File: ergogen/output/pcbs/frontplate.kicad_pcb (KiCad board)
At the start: 2 copper layers, 133.3 x 91.7 mm, 5 parts

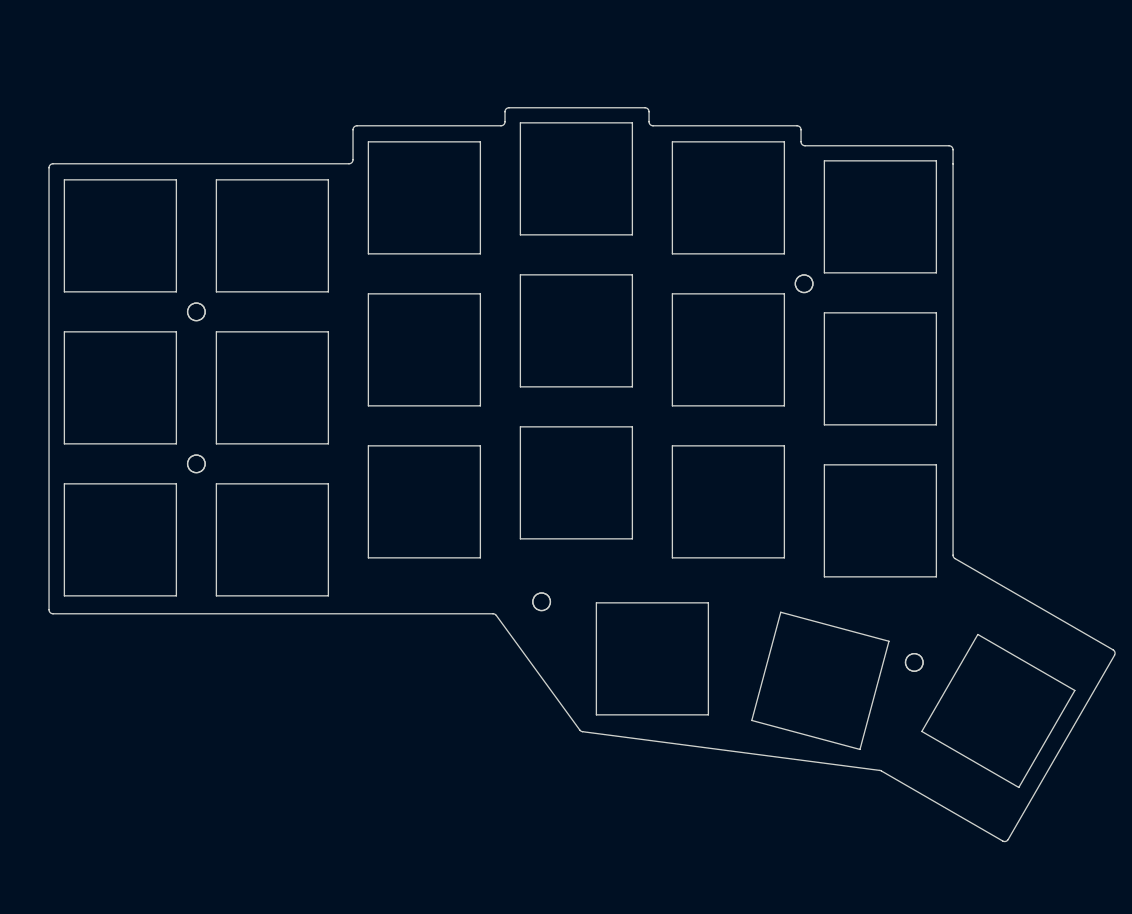
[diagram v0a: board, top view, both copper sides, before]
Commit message: Removed outer column
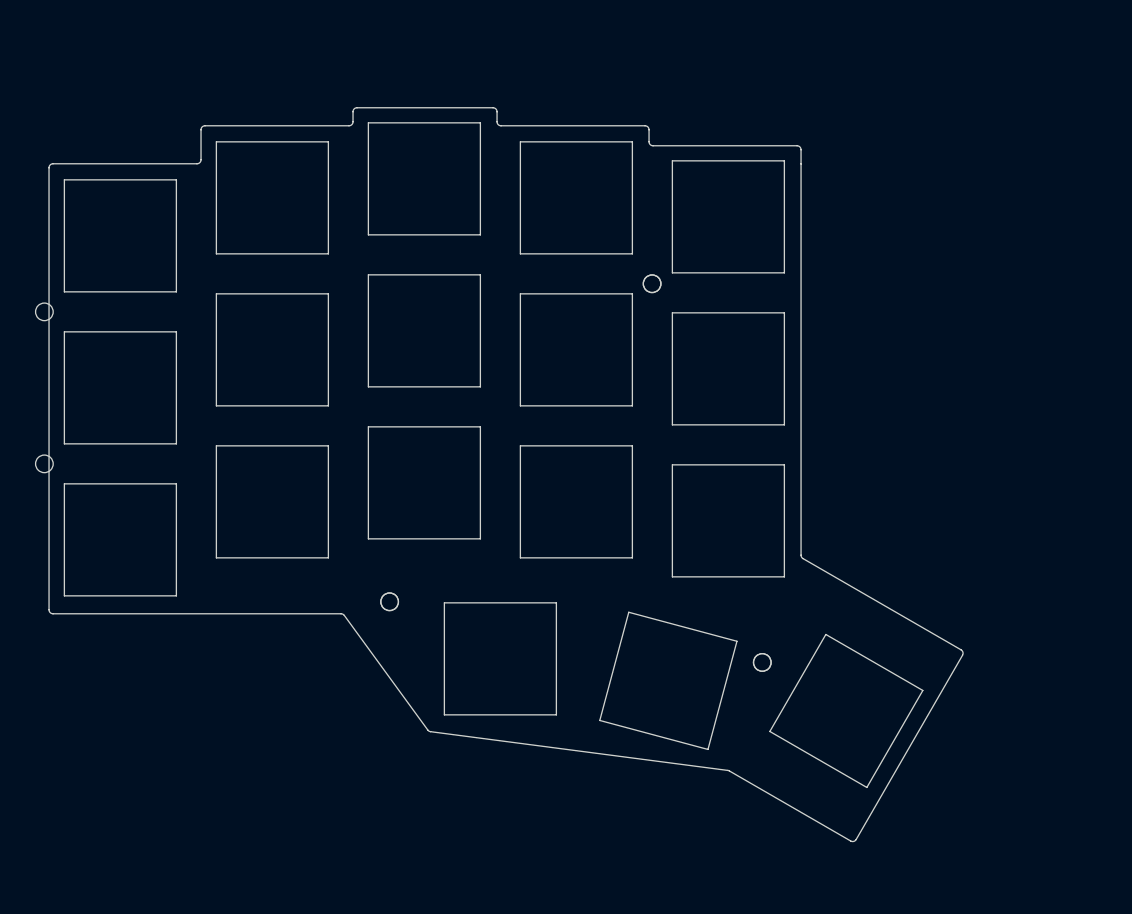
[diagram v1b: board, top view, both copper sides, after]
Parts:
- moved MH5 19.0 mm to (180.2, 115.3)
- moved MH1 19.0 mm to (90.5, 71.5)
- moved MH2 19.0 mm to (90.5, 90.5)
- moved MH3 19.0 mm to (166.5, 68.0)
- moved MH4 19.0 mm to (133.7, 107.7)
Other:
- board size 133.3 x 91.7 mm -> 114.3 x 91.7 mm

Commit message: Changed stagger to be like karia
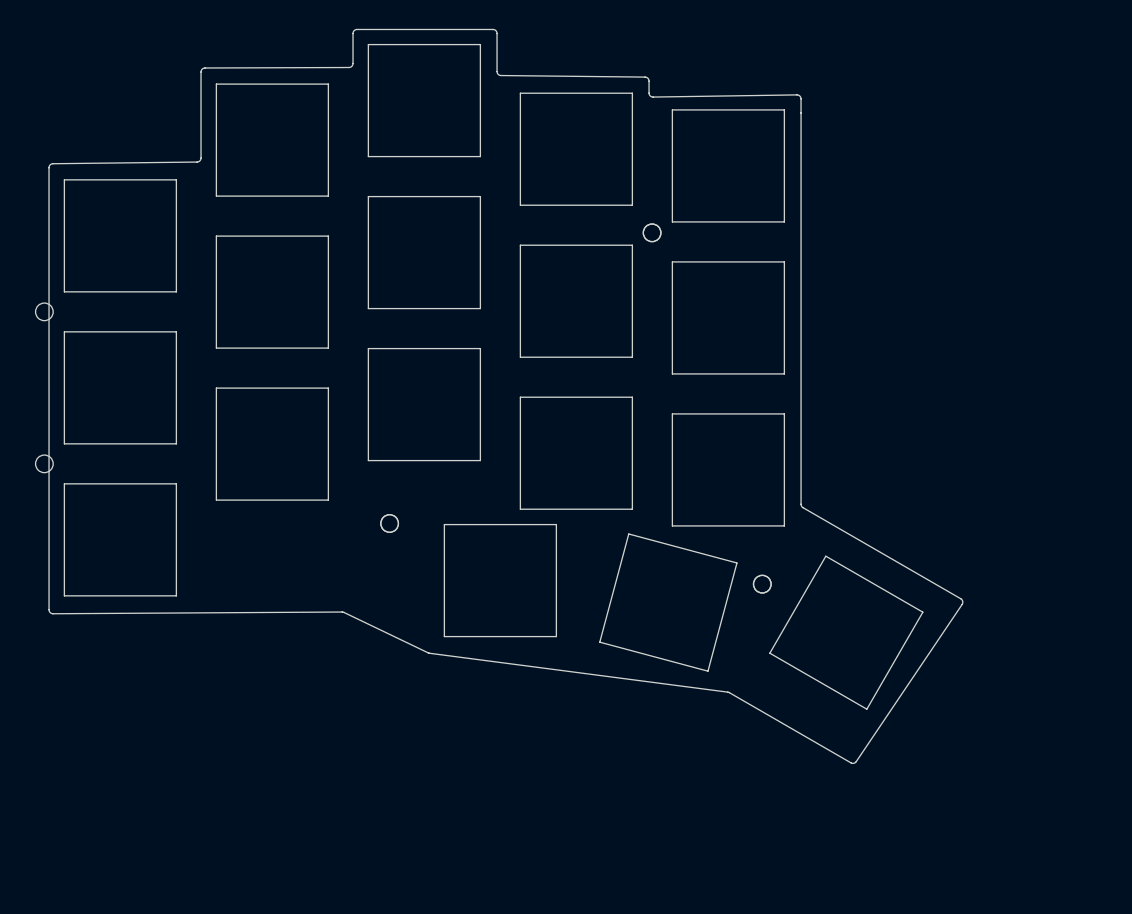
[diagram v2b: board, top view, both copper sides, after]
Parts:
- moved MH4 9.78 mm to (133.7, 98.0)
- moved MH5 9.78 mm to (180.2, 105.5)
- moved MH3 6.36 mm to (166.5, 61.6)
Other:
- board size 114.3 x 91.7 mm -> 114.2 x 91.7 mm

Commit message: Added splay to pinky
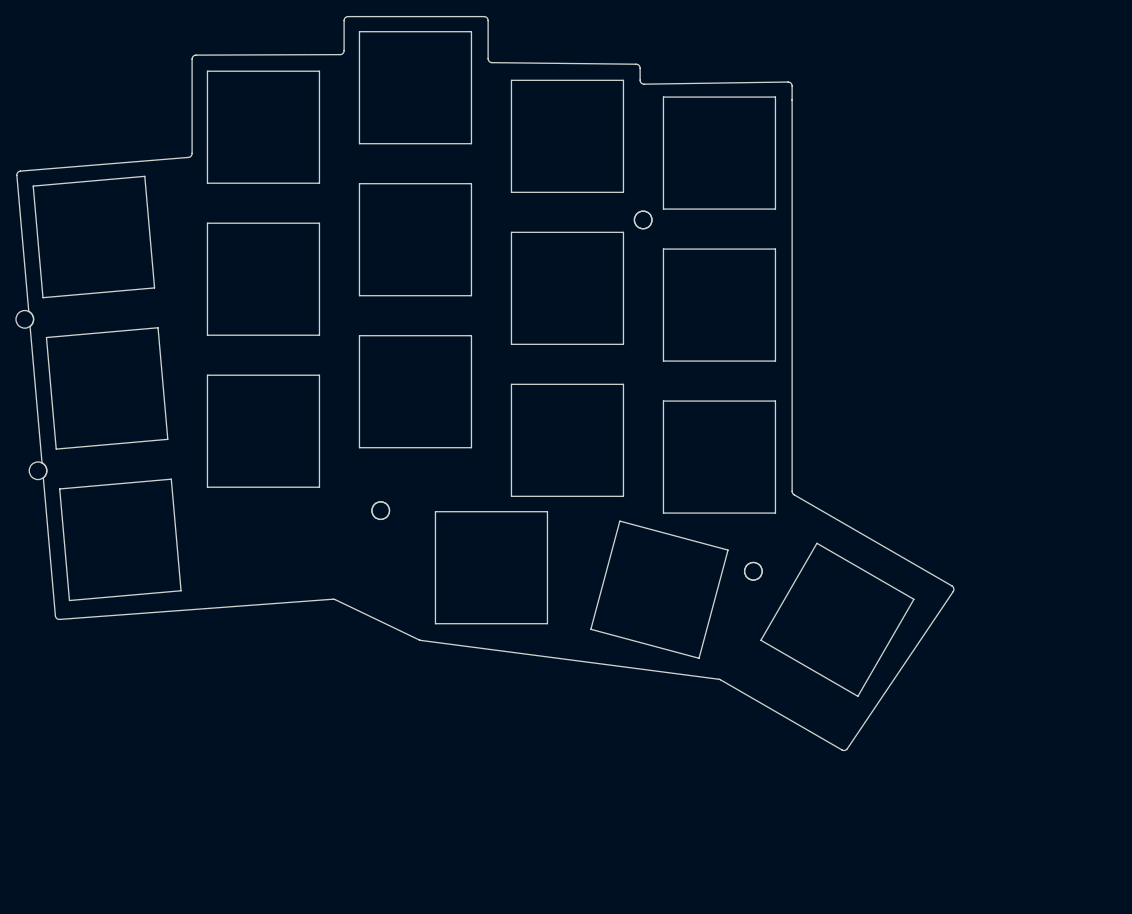
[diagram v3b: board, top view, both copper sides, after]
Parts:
- moved MH1 2.62 mm to (88.1, 72.4), turned to 5 degrees
- moved MH4 1.96 mm to (132.5, 96.3)
- moved MH5 1.96 mm to (179.1, 103.9)
- moved MH3 1.96 mm to (165.4, 60.0)
- moved MH2 1.17 mm to (89.7, 91.4), turned to 5 degrees
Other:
- board size 114.2 x 91.7 mm -> 117.1 x 91.7 mm

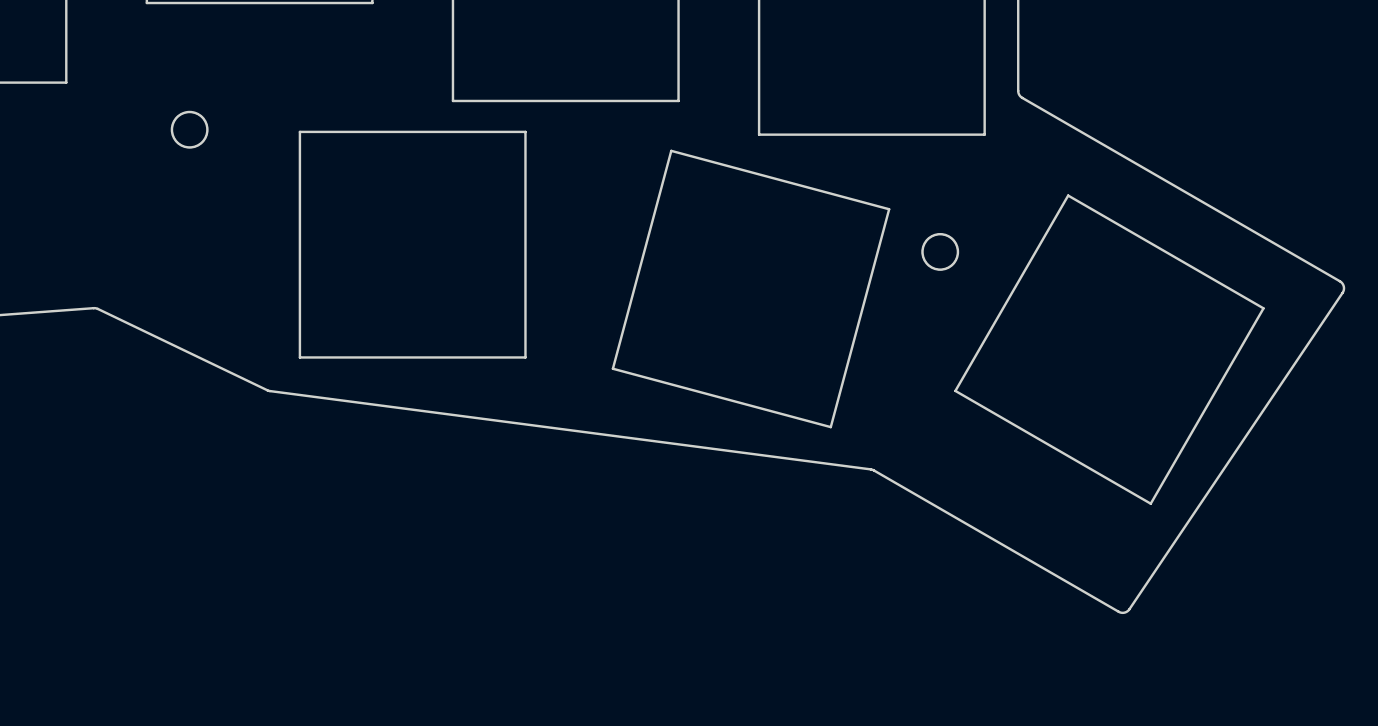
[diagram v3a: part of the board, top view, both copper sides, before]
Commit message: Changed thumb key back to 1u
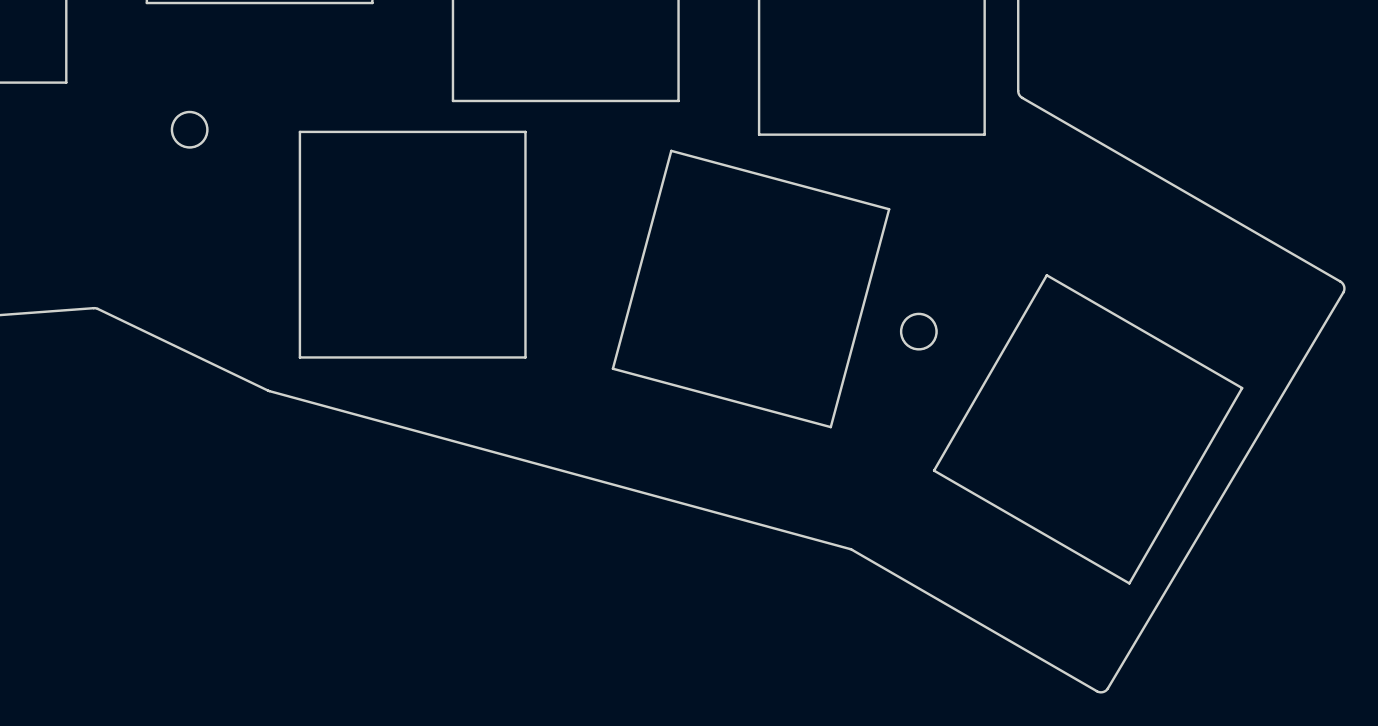
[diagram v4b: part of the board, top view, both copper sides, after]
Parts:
- moved MH5 5.12 mm to (177.8, 108.9)
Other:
- board size 117.1 x 91.7 mm -> 117.2 x 96.7 mm
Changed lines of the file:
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@@
   )
   (module "ceoloide:mounting_hole_npth" (layer F.Cu)
-      (at 179.1254966 103.9282479 60)
+      (at 177.7998255 108.87572 60)
       (fp_text reference "MH5" (at 0 2.55 60) (layer F.SilkS) hide (effects (font (size 1 1) (thickness 0.15))))
       (pad "" np_thru_hole circle (at 0 0 60) (size 2.2 2.2) (drill 2.2) (layers *.Cu *.Mask))
@@
 (gr_line (start 183.96667038015485 43.26992130873259) (end 183.96744510000002 45.01459040003829) (layer Edge.Cuts) (stroke (width 0.15) (type default)))
 (gr_line (start 183.9674451 45.01481240004068) (end 183.9674451 93.93435851661681) (layer Edge.Cuts) (stroke (width 0.15) (type default)))
-(gr_line (start 184.2174451 94.36737121661682) (end 203.93834540973833 105.75323831890144) (layer Edge.Cuts) (stroke (width 0.15) (type default)))
-(gr_line (start 204.1030141097383 106.46562511890141) (end 190.86864454351888 126.1091037392597) (layer Edge.Cuts) (stroke (width 0.15) (type default)))
-(gr_line (start 190.2039758435189 126.26274233925969) (end 175.00808706223265 117.48939183913699) (layer Edge.Cuts) (stroke (width 0.15) (type default)))
-(gr_line (start 174.82271206223268 117.42659853913699) (end 137.52391425873893 112.56494858875345) (layer Edge.Cuts) (stroke (width 0.15) (type default)))
-(gr_line (start 137.3721942392345 112.5199139793924) (end 126.84466306000907 107.46728833906016) (layer Edge.Cuts) (stroke (width 0.15) (type default)))
+(gr_line (start 184.2174451 94.36737121661682) (end 203.9637846754554 105.76792568581091) (layer Edge.Cuts) (stroke (width 0.15) (type default)))
+(gr_line (start 204.14352157545537 106.45652828581092) (end 189.53461200661957 131.0192645320555) (layer Edge.Cuts) (stroke (width 0.15) (type default)))
+(gr_line (start 188.85487510661957 131.19668733205543) (end 173.65217521437293 122.41940443517655) (layer Edge.Cuts) (stroke (width 0.15) (type default)))
+(gr_line (start 173.53339681437296 122.36994343517657) (end 137.4884527110838 112.56655937095502) (layer Edge.Cuts) (stroke (width 0.15) (type default)))
+(gr_line (start 137.40332929157935 112.53485706159397) (end 126.84466306000907 107.46728833906016) (layer Edge.Cuts) (stroke (width 0.15) (type default)))
 (gr_line (start 126.59146074050466 107.41942002969911) (end 92.41319770323031 109.94573156980263) (layer Edge.Cuts) (stroke (width 0.15) (type default)))
 (gr_arc (start 87.51811424775414 53.90547845501909) (mid 87.17664344775413 54.0812949550191) (end 87.06061104775414 54.4474235550191) (layer Edge.Cuts) (stroke (width 0.15) (type default)))
@@
 (gr_arc (start 183.9674451 45.01481240004068) (mid 183.9674451 45.014701400040686) (end 183.9674451 45.01459040004068) (layer Edge.Cuts) (stroke (width 0.15) (type default)))
 (gr_arc (start 183.9674451 93.93435851661681) (mid 184.0344324 94.18435851661681) (end 184.2174451 94.36737121661682) (layer Edge.Cuts) (stroke (width 0.15) (type default)))
-(gr_arc (start 204.1030141097383 106.46562511890143) (mid 204.1755003097383 106.07364481890143) (end 203.9383454097383 105.75323831890142) (layer Edge.Cuts) (stroke (width 0.15) (type default)))
-(gr_arc (start 190.20397584351892 126.26274233925966) (mid 190.5665820435189 126.31688453925965) (end 190.8686445435189 126.10910373925965) (layer Edge.Cuts) (stroke (width 0.15) (type default)))
-(gr_arc (start 175.00808706223268 117.48939183913699) (mid 174.91850206223268 117.44883613913699) (end 174.82271206223268 117.42659853913699) (layer Edge.Cuts) (stroke (width 0.15) (type default)))
-(gr_arc (start 137.37219425873894 112.51991398875344) (mid 137.44626115873893 112.54847228875344) (end 137.52391425873893 112.56494858875345) (layer Edge.Cuts) (stroke (width 0.15) (type default)))
+(gr_arc (start 204.14352157545537 106.4565282858109) (mid 204.19757587545539 106.0746606858109) (end 203.96378467545537 105.7679256858109) (layer Edge.Cuts) (stroke (width 0.15) (type default)))
+(gr_arc (start 188.85487510661957 131.1966873320555) (mid 189.23115280661958 131.2474658320555) (end 189.53461200661957 131.01926453205547) (layer Edge.Cuts) (stroke (width 0.15) (type default)))
+(gr_arc (start 173.65217521437293 122.41940443517655) (mid 173.59438361437293 122.39083733517656) (end 173.53339681437294 122.36994343517655) (layer Edge.Cuts) (stroke (width 0.15) (type default)))
+(gr_arc (start 137.4033293110838 112.53485707095501) (mid 137.4451696110838 112.55264527095503) (end 137.4884527110838 112.56655937095502) (layer Edge.Cuts) (stroke (width 0.15) (type default)))
 (gr_arc (start 126.84466304050464 107.46728832969912) (mid 126.72119864050464 107.42676222969911) (end 126.59146074050464 107.41942002969911) (layer Edge.Cuts) (stroke (width 0.15) (type default)))
 (gr_arc (start 91.8782446032303 109.49068746980264) (mid 92.0523782032303 109.82794416980263) (end 92.4131977032303 109.94573156980263) (layer Edge.Cuts) (stroke (width 0.15) (type default)))
@@
 (gr_line (start 175.9576591 101.2798428) (end 162.4346975 97.6563762) (layer Edge.Cuts) (stroke (width 0.15) (type default)))
 (gr_line (start 162.4346975 97.6563762) (end 158.8112309 111.1793378) (layer Edge.Cuts) (stroke (width 0.15) (type default)))
-(gr_line (start 192.1934286 119.5559257) (end 199.1934286 107.4315701) (layer Edge.Cuts) (stroke (width 0.15) (type default)))
-(gr_line (start 199.1934286 107.4315701) (end 187.069073 100.4315701) (layer Edge.Cuts) (stroke (width 0.15) (type default)))
-(gr_line (start 187.069073 100.4315701) (end 180.069073 112.5559257) (layer Edge.Cuts) (stroke (width 0.15) (type default)))
-(gr_line (start 180.069073 112.5559257) (end 192.1934286 119.5559257) (layer Edge.Cuts) (stroke (width 0.15) (type default)))
+(gr_line (start 190.8677575 124.5033978) (end 197.8677575 112.3790422) (layer Edge.Cuts) (stroke (width 0.15) (type default)))
+(gr_line (start 197.8677575 112.3790422) (end 185.7434019 105.3790422) (layer Edge.Cuts) (stroke (width 0.15) (type default)))
+(gr_line (start 185.7434019 105.3790422) (end 178.7434019 117.5033978) (layer Edge.Cuts) (stroke (width 0.15) (type default)))
+(gr_line (start 178.7434019 117.5033978) (end 190.8677575 124.5033978) (layer Edge.Cuts) (stroke (width 0.15) (type default)))
 (gr_arc (start 88.71211749999999 73.3165013) (mid 89.14802249999998 72.3405203) (end 88.54919959999998 71.4551034) (layer Edge.Cuts) (stroke (width 0.15) (type default)))
 (gr_arc (start 90.36871289999999 92.2437231) (mid 90.80398159999999 91.2682196) (end 90.2058682 90.3831623) (layer Edge.Cuts) (stroke (width 0.15) (type default)))
 (gr_circle (center 165.35244509999998 60.01059040000001) (end 166.45244509999998 60.01059040000001) (layer Edge.Cuts) (stroke (width 0.15) (type default)) (fill none))
 (gr_circle (center 132.541445 96.3445903) (end 133.641445 96.3445903) (layer Edge.Cuts) (stroke (width 0.15) (type default)) (fill none))
-(gr_circle (center 179.1254966 103.9282479) (end 180.22549659999999 103.9282479) (layer Edge.Cuts) (stroke (width 0.15) (type default)) (fill none))
+(gr_circle (center 177.7998255 108.87572) (end 178.8998255 108.87572) (layer Edge.Cuts) (stroke (width 0.15) (type default)) (fill none))
 )
